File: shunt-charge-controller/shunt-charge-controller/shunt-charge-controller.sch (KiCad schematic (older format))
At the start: 16 parts, among them J1 Rechargeable Battery, J2 Load, J3 Solar Panel, Q1 IRLZ34N, Q2 IRLZ34N, U1 MCP6042, U2 LT1004-CZ2.5

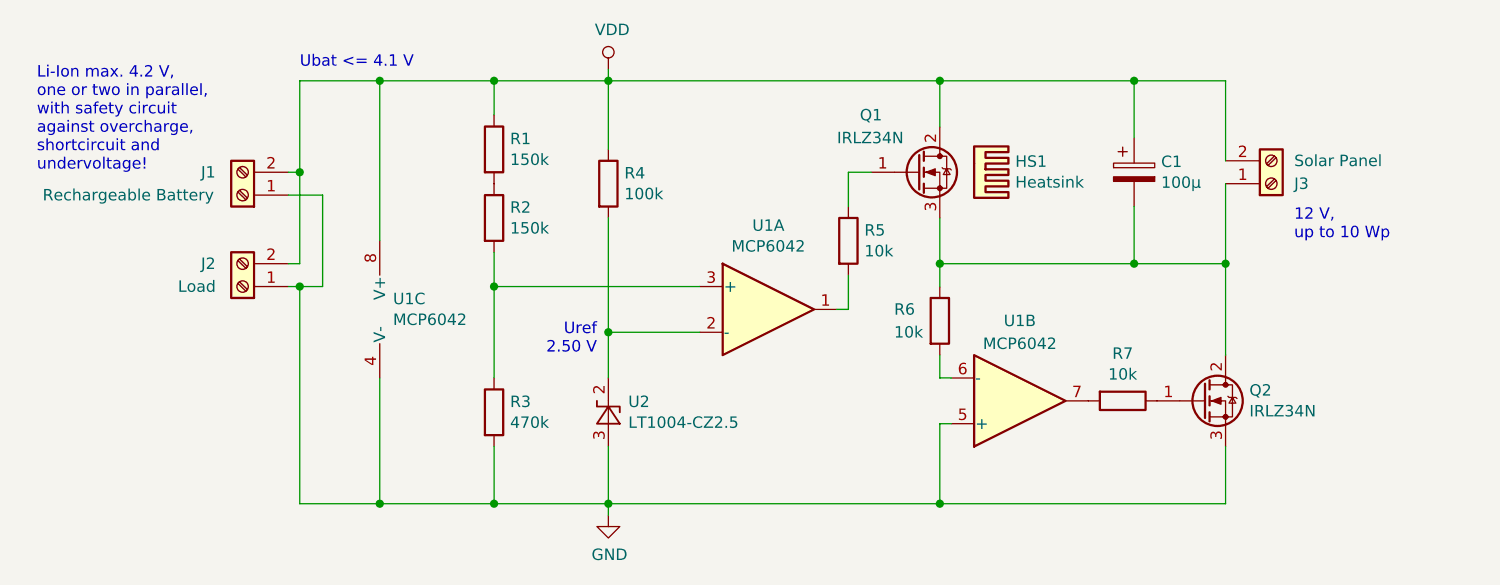
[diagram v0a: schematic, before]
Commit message: PCB layout for breadboard
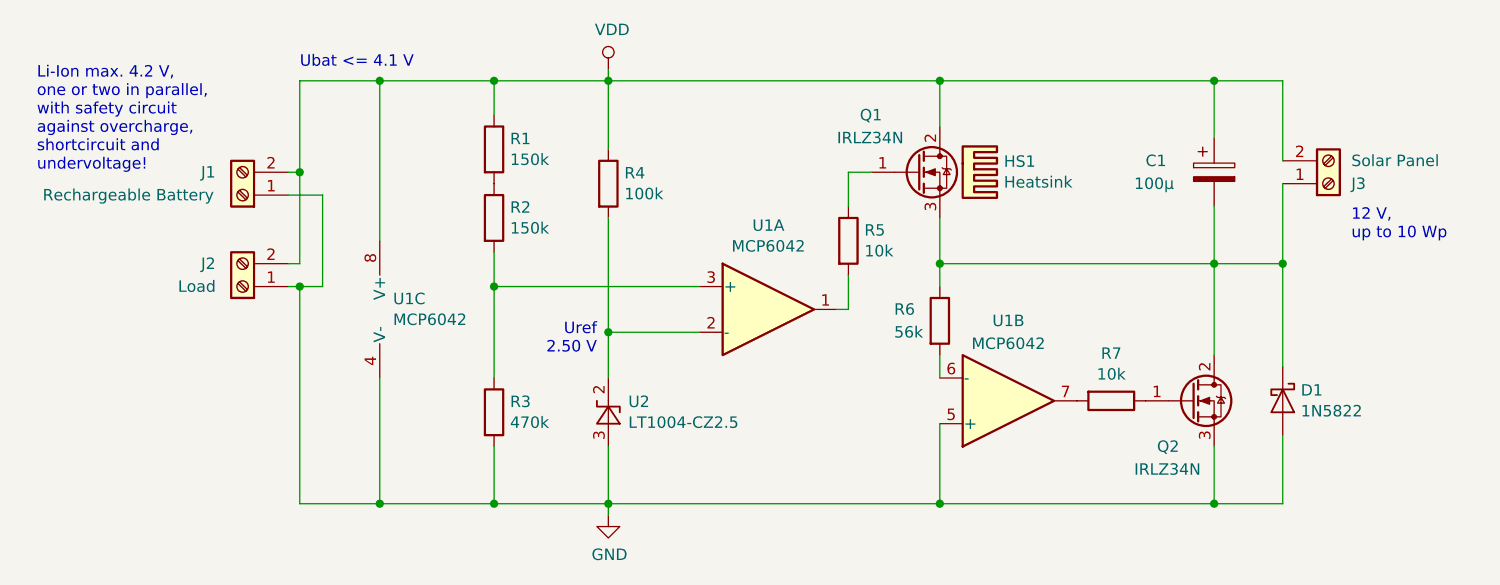
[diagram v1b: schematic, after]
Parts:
- added D1: 1N5822, Diode_THT:D_DO-201AD_P15.24mm_Horizontal, symbol Diode:1N5822
- R6: value 10k -> 56k
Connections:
- net GND: now also D1.2 (A)
- net at C1.2, J3.1 (Pin_1), Q1.3 (S)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: now also D1.1 (K)
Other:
- moved on the sheet: C1, HS1, J3, Q2, R7, U1B
